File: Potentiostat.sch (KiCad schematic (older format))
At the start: 16 parts

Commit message: Fix part info, start rough layout
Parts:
- U6: renamed from U?; footprint JetkovKiCADLib:MIC2288YD5 -> JetkovKiCADLib:SPEC-110-902
- gave numbers to parts that had none: 15
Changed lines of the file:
@@
 P 5800 4050
 AR Path="/605CEBF3" Ref="U?"  Part="1"
-AR Path="/605B4CA4/605CEBF3" Ref="U?"  Part="1"
-F 0 "U?" H 5350 5000 50  0000 C CNN
+AR Path="/605B4CA4/605CEBF3" Ref="U5"  Part="1"
+F 0 "U5" H 5350 5000 50  0000 C CNN
 F 1 "LMP91000" H 5850 5000 50  0000 C CNN
 F 2 "JetkovKiCADLib:LMP91000" H 5300 2900 50  0001 L BNN
@@
 P 5050 4700
 AR Path="/605CEBFB" Ref="#PWR?"  Part="1"
-AR Path="/605B4CA4/605CEBFB" Ref="#PWR?"  Part="1"
-F 0 "#PWR?" H 5050 4450 50  0001 C CNN
+AR Path="/605B4CA4/605CEBFB" Ref="#PWR045"  Part="1"
+F 0 "#PWR045" H 5050 4450 50  0001 C CNN
 F 1 "GND" H 5055 4527 50  0000 C CNN
 F 2 "" H 5050 4700 50  0001 C CNN
@@
 P 6650 3550
 AR Path="/605CEC09" Ref="R?"  Part="1"
-AR Path="/605B4CA4/605CEC09" Ref="R?"  Part="1"
-F 0 "R?" H 6720 3596 50  0000 L CNN
+AR Path="/605B4CA4/605CEC09" Ref="R14"  Part="1"
+F 0 "R14" H 6720 3596 50  0000 L CNN
 F 1 "49R9" H 6720 3505 50  0000 L CNN
 F 2 "JetkovKiCADLib:R_0402_NoSilk" V 6580 3550 50  0001 C CNN
@@
 P 7450 3850
 AR Path="/605CEC15" Ref="U?"  Part="1"
-AR Path="/605B4CA4/605CEC15" Ref="U?"  Part="1"
-F 0 "U?" H 7200 4200 50  0000 C CNN
+AR Path="/605B4CA4/605CEC15" Ref="U6"  Part="1"
+F 0 "U6" H 7200 4200 50  0000 C CNN
 F 1 "SPEC-110-902" H 7450 3500 50  0000 C CNN
-F 2 "JetkovKiCADLib:MIC2288YD5" H 7200 3250 50  0001 L BNN
+F 2 "JetkovKiCADLib:SPEC-110-902" H 7200 3250 50  0001 L BNN
 F 3 "http://www.spec-sensors.com/wp-content/uploads/2016/06/RESP_IRR_20-C-Package-110-902.pdf" H 7750 3400 50  0001 L BNN
 F 4 "110-902" H 7500 3150 40  0001 C CNN "Part Number"
@@
 P 6550 4300
 AR Path="/605CEC24" Ref="R?"  Part="1"
-AR Path="/605B4CA4/605CEC24" Ref="R?"  Part="1"
-F 0 "R?" H 6620 4346 50  0000 L CNN
+AR Path="/605B4CA4/605CEC24" Ref="R13"  Part="1"
+F 0 "R13" H 6620 4346 50  0000 L CNN
 F 1 "499k" H 6620 4255 50  0000 L CNN
 F 2 "JetkovKiCADLib:R_0402_NoSilk" V 6480 4300 50  0001 C CNN
@@
 P 6750 4300
 AR Path="/605CEC2A" Ref="C?"  Part="1"
-AR Path="/605B4CA4/605CEC2A" Ref="C?"  Part="1"
-F 0 "C?" H 6865 4346 50  0000 L CNN
+AR Path="/605B4CA4/605CEC2A" Ref="C15"  Part="1"
+F 0 "C15" H 6865 4346 50  0000 L CNN
 F 1 "DNP" H 6865 4255 50  0000 L CNB
 F 2 "JetkovKiCADLib:C_0402_NoSilk" H 6788 4150 50  0001 C CNN
@@
 P 4600 3450
 AR Path="/605CEC3F" Ref="C?"  Part="1"
-AR Path="/605B4CA4/605CEC3F" Ref="C?"  Part="1"
-F 0 "C?" H 4715 3496 50  0000 L CNN
+AR Path="/605B4CA4/605CEC3F" Ref="C14"  Part="1"
+F 0 "C14" H 4715 3496 50  0000 L CNN
 F 1 "1u" H 4715 3405 50  0000 L CNN
 F 2 "JetkovKiCADLib:C_0402_NoSilk" H 4638 3300 50  0001 C CNN
@@
 P 4600 3600
 AR Path="/605CEC45" Ref="#PWR?"  Part="1"
-AR Path="/605B4CA4/605CEC45" Ref="#PWR?"  Part="1"
-F 0 "#PWR?" H 4600 3350 50  0001 C CNN
+AR Path="/605B4CA4/605CEC45" Ref="#PWR044"  Part="1"
+F 0 "#PWR044" H 4600 3350 50  0001 C CNN
 F 1 "GND" H 4605 3427 50  0000 C CNN
 F 2 "" H 4600 3600 50  0001 C CNN
@@
 P 2350 3950
 AR Path="/605CEC51" Ref="U?"  Part="1"
-AR Path="/605B4CA4/605CEC51" Ref="U?"  Part="1"
-F 0 "U?" H 1900 4500 50  0000 C CNN
+AR Path="/605B4CA4/605CEC51" Ref="U4"  Part="1"
+F 0 "U4" H 1900 4500 50  0000 C CNN
 F 1 "MAX6071BAUT21T" H 2118 3695 50  0000 C CNN
 F 2 "JetkovKiCADLib:MAX6071BAUT21" H 1850 3150 50  0001 L BNN
@@
 P 2600 4100
 AR Path="/605CEC5C" Ref="#PWR?"  Part="1"
-AR Path="/605B4CA4/605CEC5C" Ref="#PWR?"  Part="1"
-F 0 "#PWR?" H 2600 3850 50  0001 C CNN
+AR Path="/605B4CA4/605CEC5C" Ref="#PWR039"  Part="1"
+F 0 "#PWR039" H 2600 3850 50  0001 C CNN
 F 1 "GND" H 2605 3927 50  0000 C CNN
 F 2 "" H 2600 4100 50  0001 C CNN
@@
 P 2900 3750
 AR Path="/605CEC62" Ref="C?"  Part="1"
-AR Path="/605B4CA4/605CEC62" Ref="C?"  Part="1"
-F 0 "C?" H 3015 3796 50  0000 L CNN
+AR Path="/605B4CA4/605CEC62" Ref="C11"  Part="1"
+F 0 "C11" H 3015 3796 50  0000 L CNN
 F 1 "0.1u" H 3015 3705 50  0000 L CNN
 F 2 "JetkovKiCADLib:C_0402_NoSilk" H 2938 3600 50  0001 C CNN
@@
 P 1000 3750
 AR Path="/605CEC69" Ref="C?"  Part="1"
-AR Path="/605B4CA4/605CEC69" Ref="C?"  Part="1"
-F 0 "C?" H 1115 3796 50  0000 L CNN
+AR Path="/605B4CA4/605CEC69" Ref="C10"  Part="1"
+F 0 "C10" H 1115 3796 50  0000 L CNN
 F 1 "0.1u" H 1115 3705 50  0000 L CNN
 F 2 "JetkovKiCADLib:C_0402_NoSilk" H 1038 3600 50  0001 C CNN
@@
 P 1000 3900
 AR Path="/605CEC6F" Ref="#PWR?"  Part="1"
-AR Path="/605B4CA4/605CEC6F" Ref="#PWR?"  Part="1"
-F 0 "#PWR?" H 1000 3650 50  0001 C CNN
+AR Path="/605B4CA4/605CEC6F" Ref="#PWR037"  Part="1"
+F 0 "#PWR037" H 1000 3650 50  0001 C CNN
 F 1 "GND" H 1005 3727 50  0000 C CNN
 F 2 "" H 1000 3900 50  0001 C CNN
@@
 P 1650 4400
 AR Path="/605CEC76" Ref="#PWR?"  Part="1"
-AR Path="/605B4CA4/605CEC76" Ref="#PWR?"  Part="1"
-F 0 "#PWR?" H 1650 4150 50  0001 C CNN
+AR Path="/605B4CA4/605CEC76" Ref="#PWR038"  Part="1"
+F 0 "#PWR038" H 1650 4150 50  0001 C CNN
 F 1 "GND" H 1655 4227 50  0000 C CNN
 F 2 "" H 1650 4400 50  0001 C CNN
@@
 P 1650 4250
 AR Path="/605CEC7C" Ref="R?"  Part="1"
-AR Path="/605B4CA4/605CEC7C" Ref="R?"  Part="1"
-F 0 "R?" H 1720 4296 50  0000 L CNN
+AR Path="/605B4CA4/605CEC7C" Ref="R11"  Part="1"
+F 0 "R11" H 1720 4296 50  0000 L CNN
 F 1 "1M" H 1720 4205 50  0000 L CNN
 F 2 "JetkovKiCADLib:R_0402_NoSilk" V 1580 4250 50  0001 C CNN
@@
 P 1000 3500
 AR Path="/605CEC87" Ref="#PWR?"  Part="1"
-AR Path="/605B4CA4/605CEC87" Ref="#PWR?"  Part="1"
-F 0 "#PWR?" H 1000 3350 50  0001 C CNN
+AR Path="/605B4CA4/605CEC87" Ref="#PWR036"  Part="1"
+F 0 "#PWR036" H 1000 3350 50  0001 C CNN
 F 1 "VDD" H 1015 3673 50  0000 C CNN
 F 2 "" H 1000 3500 50  0001 C CNN
@@
 P 3200 3750
 AR Path="/605CEC91" Ref="R?"  Part="1"
-AR Path="/605B4CA4/605CEC91" Ref="R?"  Part="1"
-F 0 "R?" H 3270 3796 50  0000 L CNN
+AR Path="/605B4CA4/605CEC91" Ref="R12"  Part="1"
+F 0 "R12" H 3270 3796 50  0000 L CNN
 F 1 "DNP" H 3270 3705 50  0000 L CNB
 F 2 "JetkovKiCADLib:R_0402_NoSilk" V 3130 3750 50  0001 C CNN
@@
 P 3200 4050
 AR Path="/605CEC97" Ref="C?"  Part="1"
-AR Path="/605B4CA4/605CEC97" Ref="C?"  Part="1"
-F 0 "C?" H 3315 4096 50  0000 L CNN
+AR Path="/605B4CA4/605CEC97" Ref="C12"  Part="1"
+F 0 "C12" H 3315 4096 50  0000 L CNN
 F 1 "DNP" H 3315 4005 50  0000 L CNB
 F 2 "JetkovKiCADLib:C_0402_NoSilk" H 3238 3900 50  0001 C CNN
@@
 P 3200 4200
 AR Path="/605CEC9D" Ref="#PWR?"  Part="1"
-AR Path="/605B4CA4/605CEC9D" Ref="#PWR?"  Part="1"
-F 0 "#PWR?" H 3200 3950 50  0001 C CNN
+AR Path="/605B4CA4/605CEC9D" Ref="#PWR041"  Part="1"
+F 0 "#PWR041" H 3200 3950 50  0001 C CNN
 F 1 "GND" H 3205 4027 50  0000 C CNN
 F 2 "" H 3200 4200 50  0001 C CNN
@@
 P 2900 3900
 AR Path="/605CECA5" Ref="#PWR?"  Part="1"
-AR Path="/605B4CA4/605CECA5" Ref="#PWR?"  Part="1"
-F 0 "#PWR?" H 2900 3650 50  0001 C CNN
+AR Path="/605B4CA4/605CECA5" Ref="#PWR040"  Part="1"
+F 0 "#PWR040" H 2900 3650 50  0001 C CNN
 F 1 "GND" H 2905 3727 50  0000 C CNN
 F 2 "" H 2900 3900 50  0001 C CNN
@@
 P 4400 3450
 AR Path="/605CECB0" Ref="C?"  Part="1"
-AR Path="/605B4CA4/605CECB0" Ref="C?"  Part="1"
-F 0 "C?" H 4515 3496 50  0000 L CNN
+AR Path="/605B4CA4/605CECB0" Ref="C13"  Part="1"
+F 0 "C13" H 4515 3496 50  0000 L CNN
 F 1 "0.1u" H 4515 3405 50  0000 L CNN
 F 2 "JetkovKiCADLib:C_0402_NoSilk" H 4438 3300 50  0001 C CNN
@@
 P 4400 3600
 AR Path="/605CECB6" Ref="#PWR?"  Part="1"
-AR Path="/605B4CA4/605CECB6" Ref="#PWR?"  Part="1"
-F 0 "#PWR?" H 4400 3350 50  0001 C CNN
+AR Path="/605B4CA4/605CECB6" Ref="#PWR043"  Part="1"
+F 0 "#PWR043" H 4400 3350 50  0001 C CNN
 F 1 "GND" H 4405 3427 50  0000 C CNN
 F 2 "" H 4400 3600 50  0001 C CNN
@@
 P 4400 3200
 AR Path="/605CECC4" Ref="#PWR?"  Part="1"
-AR Path="/605B4CA4/605CECC4" Ref="#PWR?"  Part="1"
-F 0 "#PWR?" H 4400 3050 50  0001 C CNN
+AR Path="/605B4CA4/605CECC4" Ref="#PWR042"  Part="1"
+F 0 "#PWR042" H 4400 3050 50  0001 C CNN
 F 1 "VDD" H 4415 3373 50  0000 C CNN
 F 2 "" H 4400 3200 50  0001 C CNN
@@
 P 9600 3950
 AR Path="/605CECCE" Ref="U?"  Part="1"
-AR Path="/605B4CA4/605CECCE" Ref="U?"  Part="1"
-F 0 "U?" H 9650 4250 50  0000 L CNN
+AR Path="/605B4CA4/605CECCE" Ref="U7"  Part="1"
+F 0 "U7" H 9650 4250 50  0000 L CNN
 F 1 "MCP6041T-I_OT" H 9650 4150 50  0000 L CNN
 F 2 "JetkovKiCADLib:MCP6041T-I_OT" H 9900 3550 50  0001 L BNN
@@
 P 9550 3450
 AR Path="/605CECD4" Ref="#PWR?"  Part="1"
-AR Path="/605B4CA4/605CECD4" Ref="#PWR?"  Part="1"
-F 0 "#PWR?" H 9550 3300 50  0001 C CNN
+AR Path="/605B4CA4/605CECD4" Ref="#PWR046"  Part="1"
+F 0 "#PWR046" H 9550 3300 50  0001 C CNN
 F 1 "VDD" H 9565 3623 50  0000 C CNN
 F 2 "" H 9550 3450 50  0001 C CNN
@@
 P 9550 4300
 AR Path="/605CECDA" Ref="#PWR?"  Part="1"
-AR Path="/605B4CA4/605CECDA" Ref="#PWR?"  Part="1"
-F 0 "#PWR?" H 9550 4050 50  0001 C CNN
+AR Path="/605B4CA4/605CECDA" Ref="#PWR047"  Part="1"
+F 0 "#PWR047" H 9550 4050 50  0001 C CNN
 F 1 "GND" H 9555 4127 50  0000 C CNN
 F 2 "" H 9550 4300 50  0001 C CNN
@@
 P 10050 3500
 AR Path="/605CECE8" Ref="C?"  Part="1"
-AR Path="/605B4CA4/605CECE8" Ref="C?"  Part="1"
-F 0 "C?" V 9800 3450 50  0000 L CNN
+AR Path="/605B4CA4/605CECE8" Ref="C16"  Part="1"
+F 0 "C16" V 9800 3450 50  0000 L CNN
 F 1 "0.1u" V 9900 3400 50  0000 L CNN
 F 2 "JetkovKiCADLib:C_0402_NoSilk" H 10088 3350 50  0001 C CNN
@@
 P 10450 3550
 AR Path="/605CECEE" Ref="#PWR?"  Part="1"
-AR Path="/605B4CA4/605CECEE" Ref="#PWR?"  Part="1"
-F 0 "#PWR?" H 10450 3300 50  0001 C CNN
+AR Path="/605B4CA4/605CECEE" Ref="#PWR048"  Part="1"
+F 0 "#PWR048" H 10450 3300 50  0001 C CNN
 F 1 "GND" H 10455 3377 50  0000 C CNN
 F 2 "" H 10450 3550 50  0001 C CNN
@@
 P 9050 4150
 AR Path="/605CECFA" Ref="R?"  Part="1"
-AR Path="/605B4CA4/605CECFA" Ref="R?"  Part="1"
-F 0 "R?" H 9120 4196 50  0000 L CNN
+AR Path="/605B4CA4/605CECFA" Ref="R15"  Part="1"
+F 0 "R15" H 9120 4196 50  0000 L CNN
 F 1 "DNP" H 9120 4105 50  0000 L CNB
 F 2 "JetkovKiCADLib:R_0402_NoSilk" V 8980 4150 50  0001 C CNN

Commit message: Review
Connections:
- net SPEC_WE: now reaches U5.12 (WE), U6.1 (WE), U6.10 (WE)
- net SPEC_RE: now reaches U5.13 (RE), U6.5 (RE)
- net CE: now reaches R14.2, U5.14 (CE)
- net SPEC_CE: now reaches R14.1, U6.6 (CE)
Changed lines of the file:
@@
 Text Notes 7100 3200 0    79   ~ 0
 Gas Sensor
+Text Label 6300 3950 0    40   ~ 0
+SPEC_WE
+Text Label 6300 3850 0    40   ~ 0
+SPEC_RE
+Text Label 6750 3350 0    40   ~ 0
+SPEC_CE
+Text Label 6300 3750 0    40   ~ 0
+CE
 $EndSCHEMATC

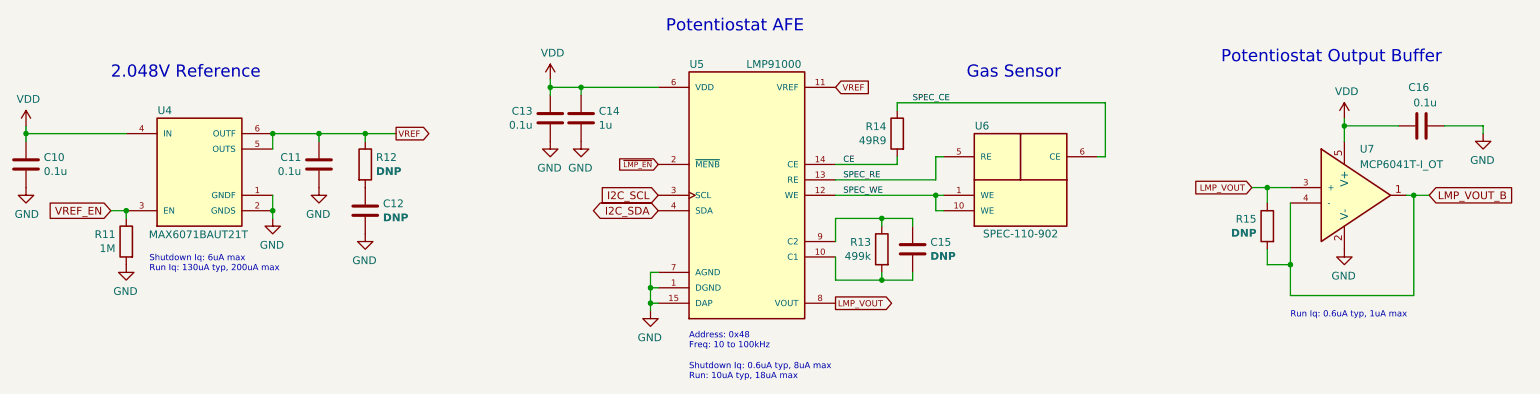
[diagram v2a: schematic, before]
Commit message: Review everything, ready for layout
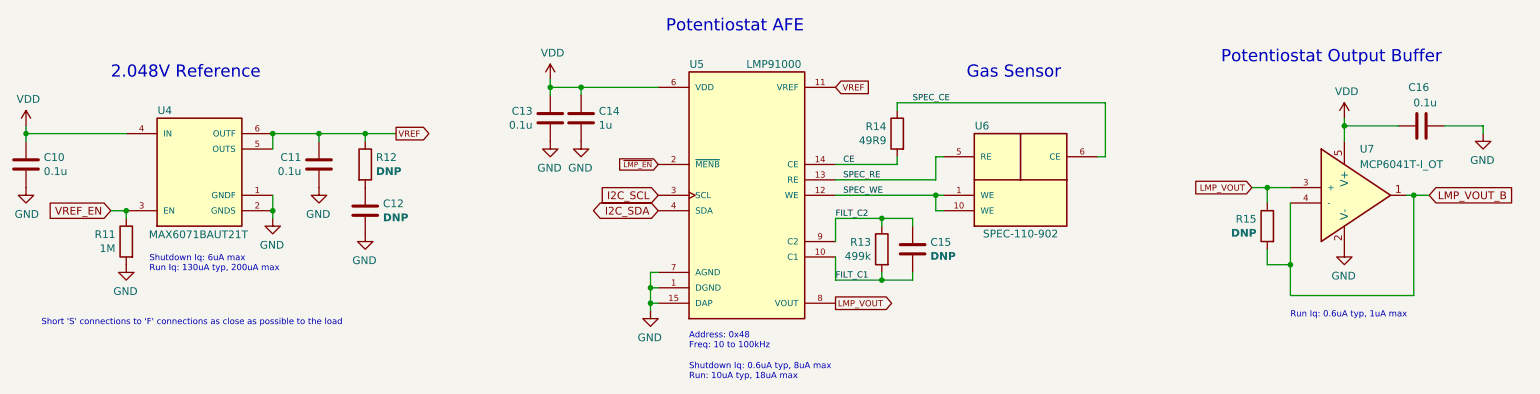
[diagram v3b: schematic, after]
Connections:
- net FILT_C1: now reaches C15.2, R13.2, U5.10 (C1)
- net FILT_C2: now reaches C15.1, R13.1, U5.9 (C2)
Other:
- note added: "Short 'S' connections to 'F' connections as close as possible to the load"
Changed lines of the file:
@@
 Text Label 6300 3750 0    40   ~ 0
 CE
+Text Notes 1100 4800 0    40   ~ 0
+Short 'S' connections to 'F' connections as close as possible to the load
+Text Label 6250 4100 0    40   ~ 0
+FILT_C2
+Text Label 6250 4500 0    40   ~ 0
+FILT_C1
 $EndSCHEMATC
